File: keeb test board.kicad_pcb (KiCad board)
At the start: 2 copper layers, 60 x 100 mm, 60 parts, among them SW1 SW_Push, SW10 SW_Push, SW11 SW_Push, SW12 SW_Push, SW13 SW_Push, SW14 SW_Push, SW15 SW_Push, SW2 SW_Push, SW3 SW_Push, SW4 SW_Push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

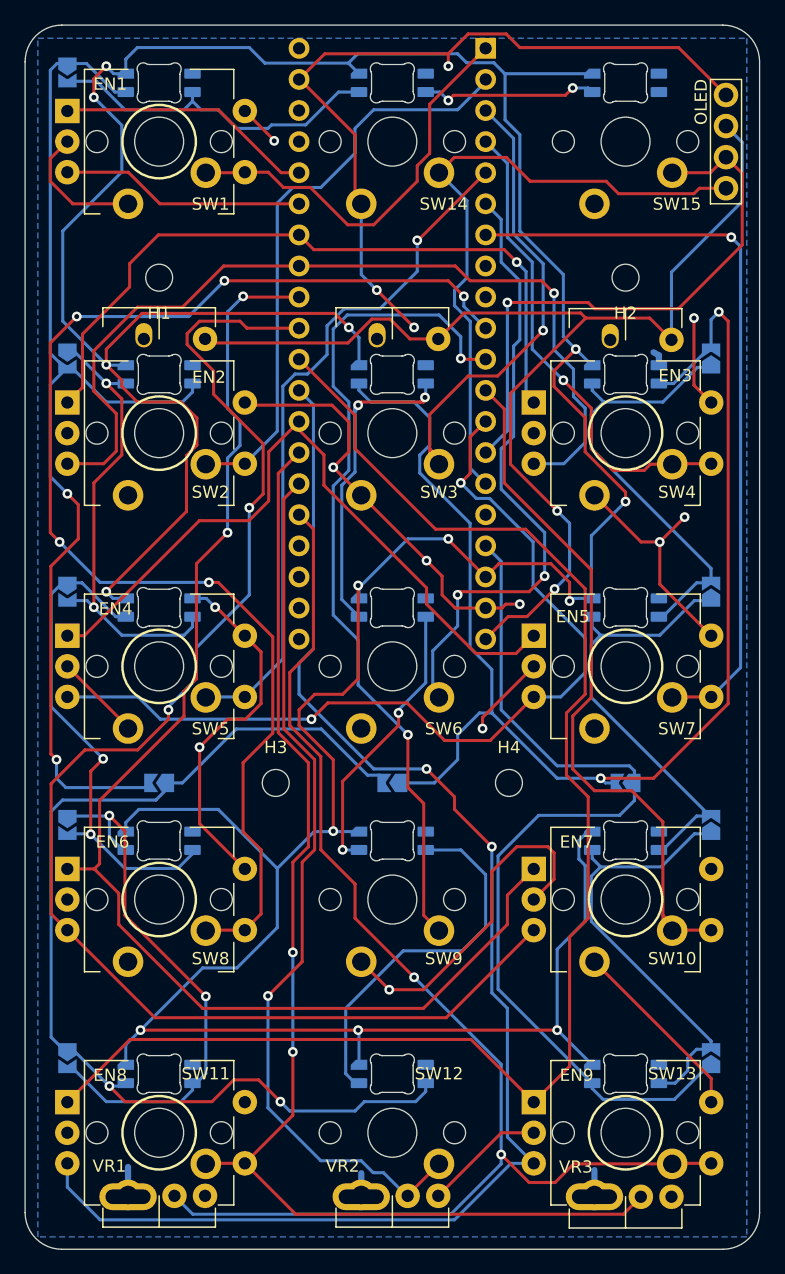
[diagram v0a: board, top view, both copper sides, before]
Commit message: move MCU downwards to better fit within new 100mm size
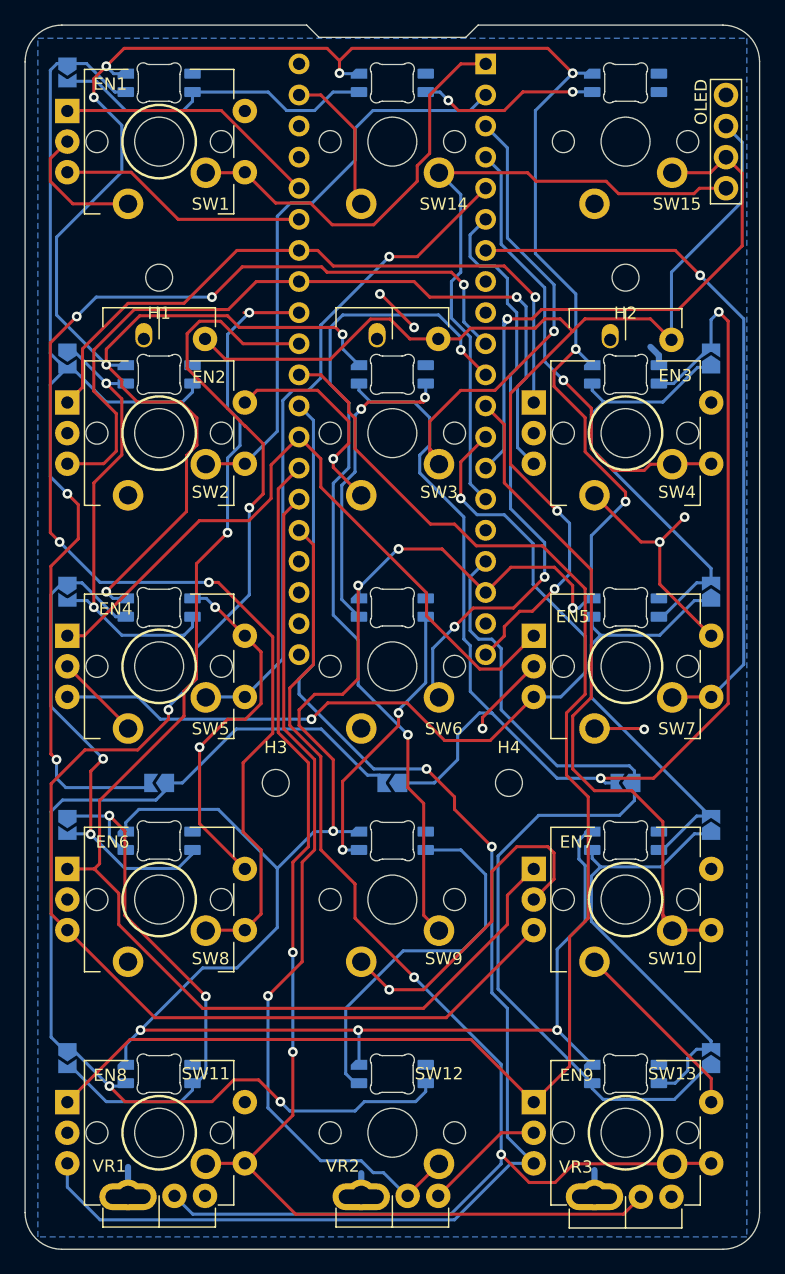
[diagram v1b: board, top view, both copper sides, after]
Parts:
- moved U1 1.27 mm to (99.8, 60.2)
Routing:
- net GND: track 244.1 -> 172.2 mm, vias 14 -> 10
- net ENC2B: track 72.9 -> 65.6 mm
- net KEY7: track 62.2 -> 58.5 mm
- net ENC2A: track 59.0 -> 55.5 mm
- net KEY10: track 58.3 -> 55.4 mm
- net KEY8: track 106.3 -> 109.0 mm
- net KEY6: track 50.8 -> 48.5 mm
- net +5V: track 337.2 -> 339.2 mm, vias 14 -> 16
- net Net-(D8-Pad1): track 88.0 -> 86.1 mm
- net KEY5: track 56.5 -> 54.9 mm
- net Net-(D5-Pad1): track 27.0 -> 25.6 mm
- net KEY12-POT2: track 72.2 -> 70.8 mm
- net KEY13-POT3: track 109.2 -> 107.9 mm
- net KEY4: track 39.4 -> 38.1 mm
- net KEY11-POT1: track 99.8 -> 98.5 mm
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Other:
- outline, holes or cut-outs redrawn

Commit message: Routing improvements
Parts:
- H1, H2, H3, H4: footprint MountingHole:MountingHole_2.2mm_M2_DIN965 -> Keeby-Cat Footprints:MountingHole_2.2mm_M2_DIN965
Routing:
- net GND: track 172.2 -> 95.8 mm, vias 10 -> 3
- net ENC4B: track 115.9 -> 103.0 mm
- net LED_DATA: track 75.7 -> 67.6 mm
- net ENC3B: track 72.8 -> 66.6 mm
- net ENC3A: track 57.9 -> 62.7 mm
- net ENC5A: track 120.0 -> 123.0 mm
- net KEY9: track 69.8 -> 72.5 mm
- net KEY1: track 33.6 -> 30.9 mm, vias 0 -> 1
- net KEY12-POT2: track 70.8 -> 68.2 mm, vias 1 -> 2
- net KEY6: track 48.5 -> 46.3 mm
- net ENC5B: track 116.4 -> 115.0 mm
- net Net-(D12-Pad1): track 88.5 -> 89.8 mm
- net KEY7: track 58.5 -> 57.3 mm
- net Net-(D4-Pad1): track 111.4 -> 110.3 mm, vias 2 -> 3
- net SCL-SW: track 48.0 -> 48.7 mm
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
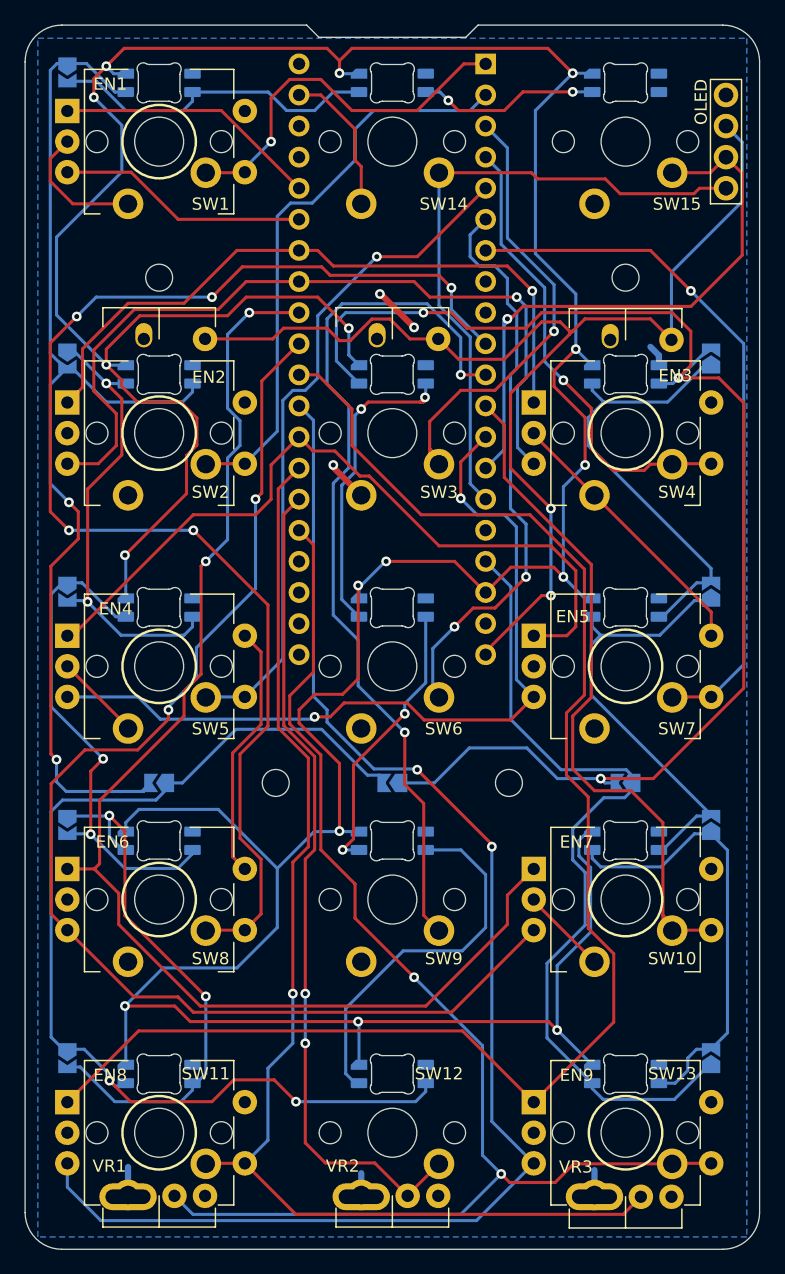
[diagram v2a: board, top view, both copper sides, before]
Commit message: Fixed pin-sharing faders/keys
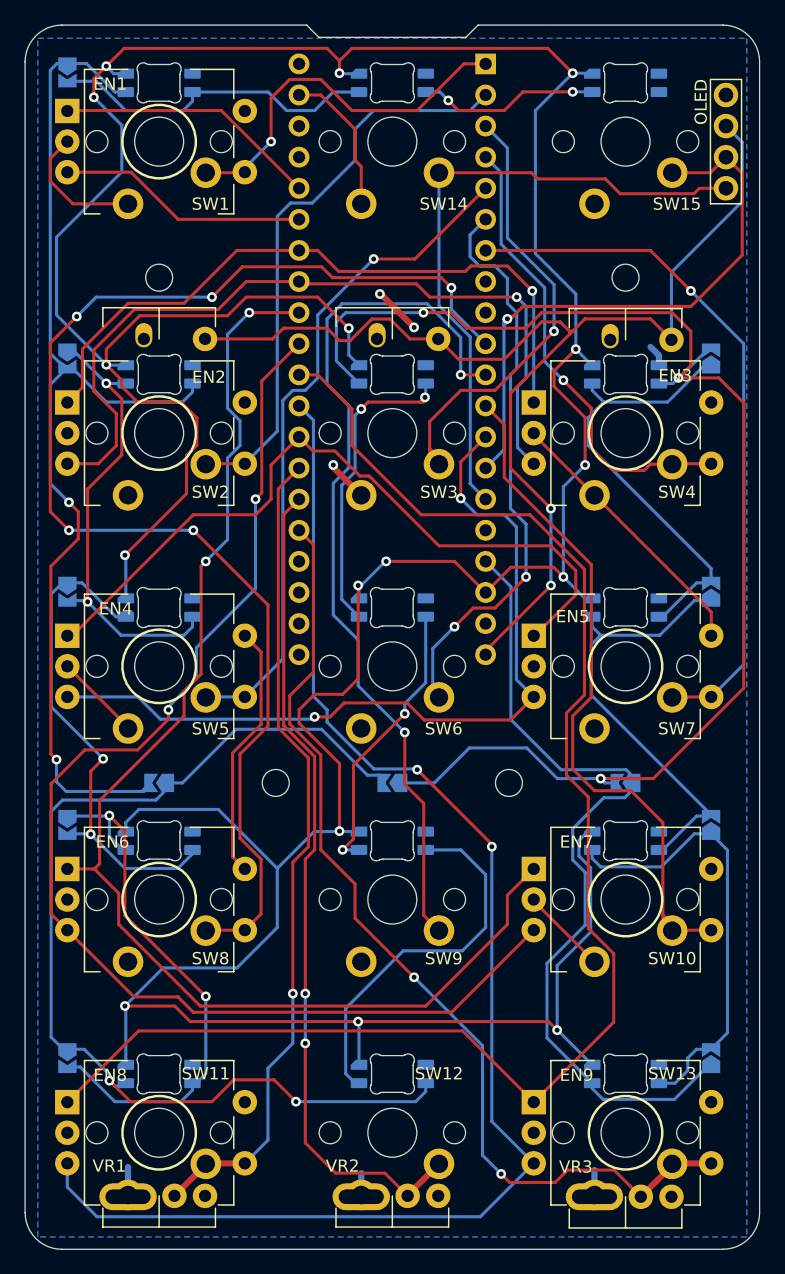
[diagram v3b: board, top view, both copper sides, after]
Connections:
- VR1 pad 2B: KEY13-POT3 -> KEY11-POT1
- VR3 pad 2B: KEY11-POT1 -> KEY13-POT3
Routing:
- net KEY11-POT1: track 98.5 -> 67.5 mm
- net KEY13-POT3: track 107.7 -> 80.9 mm
- net ENC3A: track 62.7 -> 61.2 mm

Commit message: removed extra via
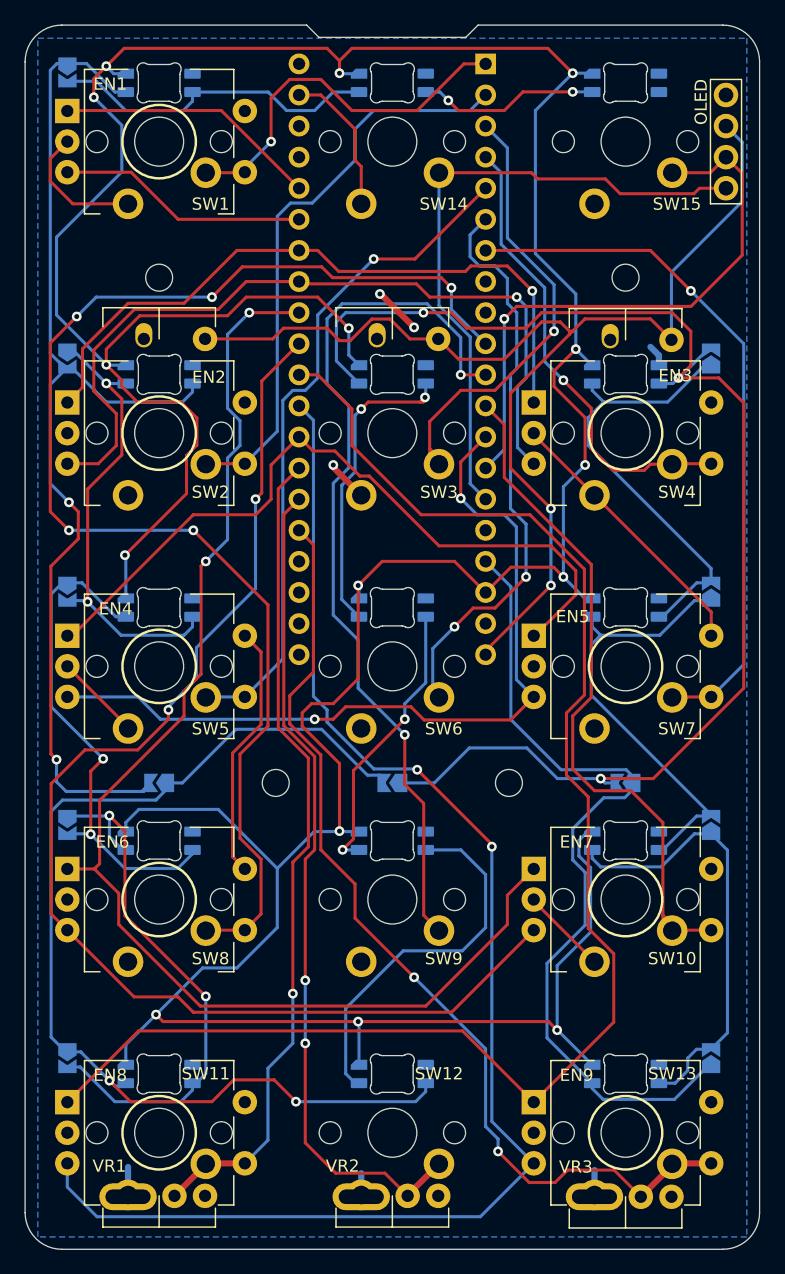
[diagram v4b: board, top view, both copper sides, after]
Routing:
- net +5V: track 338.5 -> 333.2 mm, vias 16 -> 15
- net KEY13-POT3: track 80.9 -> 80.0 mm
- net SCL-SW: track 48.7 -> 47.9 mm
- net Net-(D8-Pad1): track 86.4 -> 85.6 mm

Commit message: more copper
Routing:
- net Net-(D12-Pad1): track 89.8 -> 87.0 mm
- net +3V3: track 96.4 -> 98.3 mm
- net +5V: track 333.2 -> 331.6 mm
- net Net-(D4-Pad1): track 110.3 -> 108.9 mm
- net Net-(D10-Pad3): track 44.5 -> 43.6 mm
- net KEY13-POT3: track 80.0 -> 79.2 mm
- net KEY8: track 108.4 -> 107.7 mm

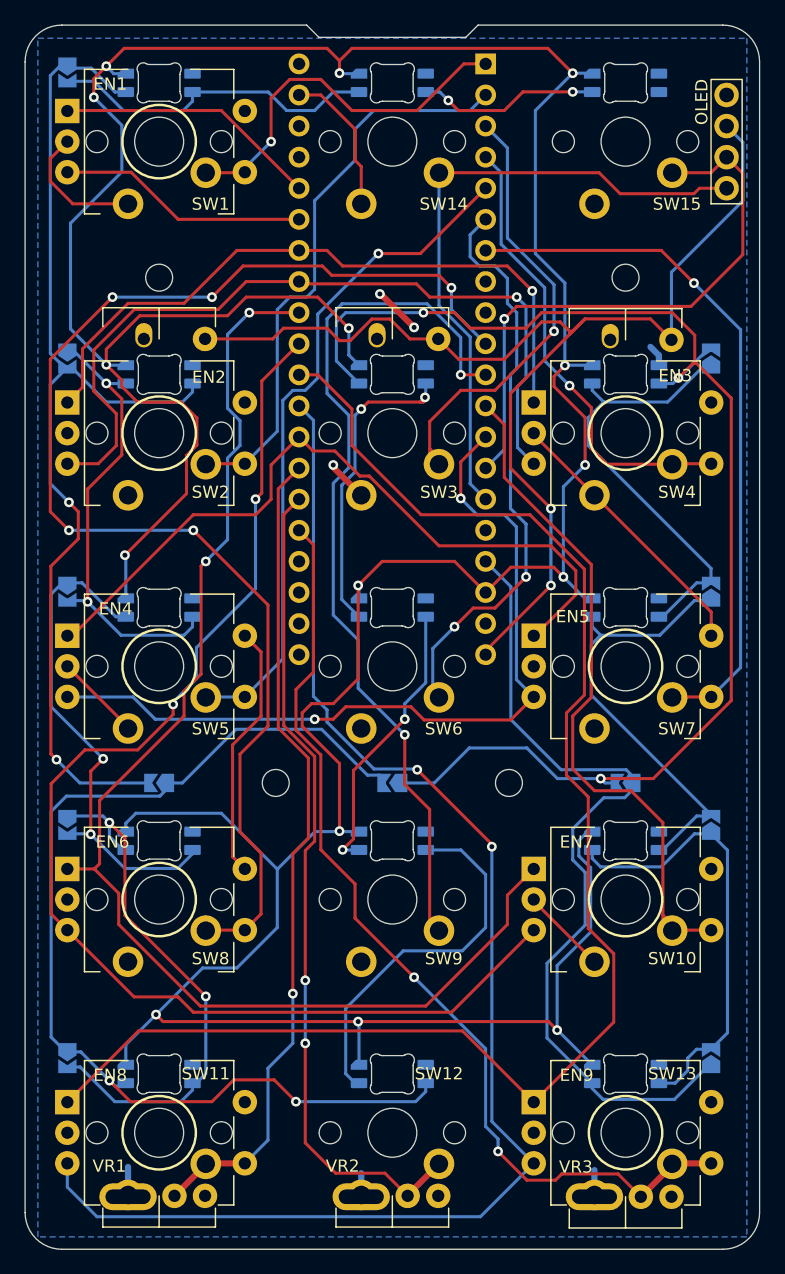
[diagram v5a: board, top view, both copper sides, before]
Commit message: Centered faders and rotated LEDs
Experimental solution to make faders centered to lower 4 rows of keys/grid. Requires bending or trimming off an unused pin from the faders.
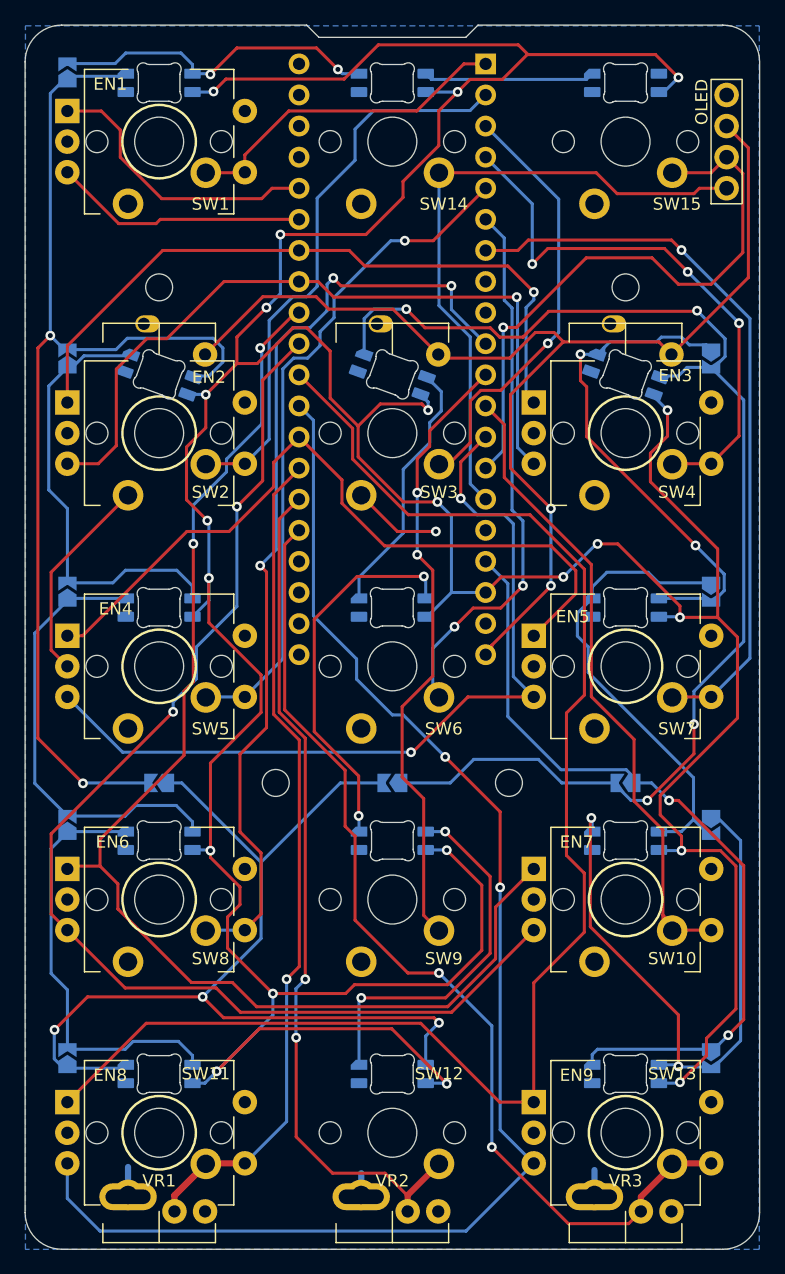
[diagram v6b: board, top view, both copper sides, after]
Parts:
- D1, D10, D11, D13, D14, D15, D2, D3, D6, D7, D8, D9: value SK6812MINI -> SK6812MINI-E; footprint marbastlib-mx:LED_MX_6028R_lower-offset -> Keeby-Cat Footprints:LED_MX_SK6812MINI-E
- D12, D4, D5: value SK6812MINI -> SK6812MINI-E; footprint marbastlib-mx:LED_MX_6028R_lower-offset -> Keeby-Cat Footprints:LED_MX_SK6812MINI-E_rotated
- VR1, VR2, VR3: value L_POT_Dual_PS60M -> L_POT_Dual_PS60M_combo
- moved VR3 33.8 mm to (111.2, 119.0)
- moved VR1 33.7 mm to (73.1, 119.0)
- moved VR2 33.7 mm to (92.2, 119.0)
- moved H1 0.79 mm to (73.1, 78.5)
- moved H2 0.79 mm to (111.2, 78.5)
- turned JP1 to -90 degrees
- turned JP10 to 90 degrees
- turned JP11 to 90 degrees
- turned JP12 to 90 degrees
- turned JP13 to 90 degrees
- turned JP2 to -90 degrees
- turned JP3 to -90 degrees
- turned JP4 to -90 degrees
- turned JP9 to 90 degrees
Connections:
- D1 pad 1: Net-(D1-Pad1) -> +5V
- D1 pad 2: GND -> Net-(D1-Pad2)
- D1 pad 3: LED_DATA -> GND
- D1 pad 4: +5V -> LED_DATA
- D10 pad 1: Net-(D10-Pad1) -> +5V
- D10 pad 2: GND -> Net-(D10-Pad2)
- D10 pad 3: Net-(D10-Pad3) -> GND
- D10 pad 4: +5V -> Net-(D10-Pad4)
- D11 pad 1: Net-(D11-Pad1) -> +5V
- D11 pad 2: GND -> Net-(D11-Pad2)
- D11 pad 3: Net-(D10-Pad1) -> GND
- D11 pad 4: +5V -> Net-(D10-Pad2)
- D12 pad 1: Net-(D12-Pad1) -> +5V
- D12 pad 2: GND -> Net-(D12-Pad2)
- D12 pad 3: Net-(D11-Pad1) -> GND
- D12 pad 4: +5V -> Net-(D11-Pad2)
- D13 pad 1: Net-(D13-Pad1) -> +5V
- D13 pad 2: GND -> Net-(D13-Pad2)
- D13 pad 3: Net-(D12-Pad1) -> GND
- D13 pad 4: +5V -> Net-(D12-Pad2)
- D14 pad 1: Net-(D14-Pad1) -> +5V
- D14 pad 2: GND -> Net-(D14-Pad2)
- D14 pad 3: Net-(D13-Pad1) -> GND
- D14 pad 4: +5V -> Net-(D13-Pad2)
- D15 pad 1: unconnected-(D15-Pad1) -> +5V
- D15 pad 2: GND -> unconnected-(D15-Pad2)
- D15 pad 3: Net-(D14-Pad1) -> GND
- D15 pad 4: +5V -> Net-(D14-Pad2)
- D2 pad 1: Net-(D2-Pad1) -> +5V
- D2 pad 2: GND -> Net-(D2-Pad2)
- D2 pad 3: Net-(D1-Pad1) -> GND
- D2 pad 4: +5V -> Net-(D1-Pad2)
- D3 pad 1: Net-(D3-Pad1) -> +5V
- D3 pad 2: GND -> Net-(D3-Pad2)
- D3 pad 3: Net-(D2-Pad1) -> GND
- D3 pad 4: +5V -> Net-(D2-Pad2)
- D4 pad 1: Net-(D4-Pad1) -> +5V
- D4 pad 2: GND -> Net-(D4-Pad2)
- D4 pad 3: Net-(D3-Pad1) -> GND
- D4 pad 4: +5V -> Net-(D3-Pad2)
- D5 pad 1: Net-(D5-Pad1) -> +5V
- D5 pad 2: GND -> Net-(D5-Pad2)
- D5 pad 3: Net-(D4-Pad1) -> GND
- D5 pad 4: +5V -> Net-(D4-Pad2)
- D6 pad 1: Net-(D6-Pad1) -> +5V
- D6 pad 2: GND -> Net-(D6-Pad2)
- D6 pad 3: Net-(D5-Pad1) -> GND
- D6 pad 4: +5V -> Net-(D5-Pad2)
- D7 pad 1: Net-(D7-Pad1) -> +5V
- D7 pad 2: GND -> Net-(D7-Pad2)
- D7 pad 3: Net-(D6-Pad1) -> GND
- D7 pad 4: +5V -> Net-(D6-Pad2)
- D8 pad 1: Net-(D8-Pad1) -> +5V
- D8 pad 2: GND -> Net-(D8-Pad2)
- D8 pad 3: Net-(D7-Pad1) -> GND
- D8 pad 4: +5V -> Net-(D7-Pad2)
- D9 pad 1: Net-(D10-Pad3) -> +5V
- D9 pad 2: GND -> Net-(D10-Pad4)
- D9 pad 3: Net-(D8-Pad1) -> GND
- D9 pad 4: +5V -> Net-(D8-Pad2)
- JP1 pad 2: Net-(D1-Pad1) -> Net-(D1-Pad2)
- JP10 pad 1: Net-(D10-Pad3) -> Net-(D10-Pad4)
- JP10 pad 2: Net-(D10-Pad1) -> Net-(D10-Pad2)
- JP11 pad 1: Net-(D10-Pad1) -> Net-(D10-Pad2)
- JP11 pad 2: Net-(D11-Pad1) -> Net-(D11-Pad2)
- JP12 pad 1: Net-(D11-Pad1) -> Net-(D11-Pad2)
- JP12 pad 2: Net-(D12-Pad1) -> Net-(D12-Pad2)
- JP13 pad 1: Net-(D12-Pad1) -> Net-(D12-Pad2)
- JP13 pad 2: Net-(D13-Pad1) -> Net-(D13-Pad2)
- JP2 pad 1: Net-(D1-Pad1) -> Net-(D1-Pad2)
- JP2 pad 2: Net-(D2-Pad1) -> Net-(D2-Pad2)
- JP3 pad 1: Net-(D2-Pad1) -> Net-(D2-Pad2)
- JP3 pad 2: Net-(D3-Pad1) -> Net-(D3-Pad2)
- JP4 pad 1: Net-(D3-Pad1) -> Net-(D3-Pad2)
- JP4 pad 2: Net-(D4-Pad1) -> Net-(D4-Pad2)
- JP9 pad 1: Net-(D8-Pad1) -> Net-(D8-Pad2)
- JP9 pad 2: Net-(D10-Pad3) -> Net-(D10-Pad4)
- JPF1 pad 2: Net-(D4-Pad1) -> Net-(D4-Pad2)
- JPF2 pad 1: Net-(D4-Pad1) -> Net-(D4-Pad2)
- JPF2 pad 2: Net-(D8-Pad1) -> Net-(D8-Pad2)
- JPF3 pad 1: Net-(D8-Pad1) -> Net-(D8-Pad2)
- JPF3 pad 2: Net-(D12-Pad1) -> Net-(D12-Pad2)
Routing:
- net Net-(D4-Pad1): track 108.9 -> 0.00 mm, vias 3 -> 0
- net Net-(D4-Pad2): track 0.00 -> 105.2 mm, vias 0 -> 4
- net Net-(D12-Pad2): track 0.00 -> 90.0 mm, vias 0 -> 2
- net Net-(D12-Pad1): track 87.0 -> 0.00 mm, vias 2 -> 0
- net Net-(D8-Pad1): track 86.0 -> 0.00 mm, vias 2 -> 0
- net Net-(D8-Pad2): track 0.00 -> 81.9 mm, vias 0 -> 3
- net GND: track 95.8 -> 30.5 mm, vias 3 -> 1
- net Net-(D1-Pad2): track 0.00 -> 51.7 mm, vias 0 -> 2
- net Net-(D10-Pad3): track 43.6 -> 0.00 mm, vias 2 -> 0
- net Net-(D3-Pad2): track 0.00 -> 42.1 mm, vias 0 -> 2
- net Net-(D10-Pad1): track 41.6 -> 0.00 mm, vias 2 -> 0
- net Net-(D2-Pad2): track 0.00 -> 39.1 mm
- net Net-(D11-Pad1): track 37.5 -> 0.00 mm, vias 2 -> 0
- net Net-(D11-Pad2): track 0.00 -> 36.7 mm
- net Net-(D10-Pad2): track 0.00 -> 36.6 mm
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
